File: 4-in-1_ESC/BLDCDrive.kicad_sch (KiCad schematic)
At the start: 26 parts, among them Q13 BSC070N10NS3G, Q14 BSC070N10NS3G, Q21 BSC070N10NS3G, Q22 BSC070N10NS3G, Q5 BSC070N10NS3G, Q9 BSC070N10NS3G, U1 JSM6288Q

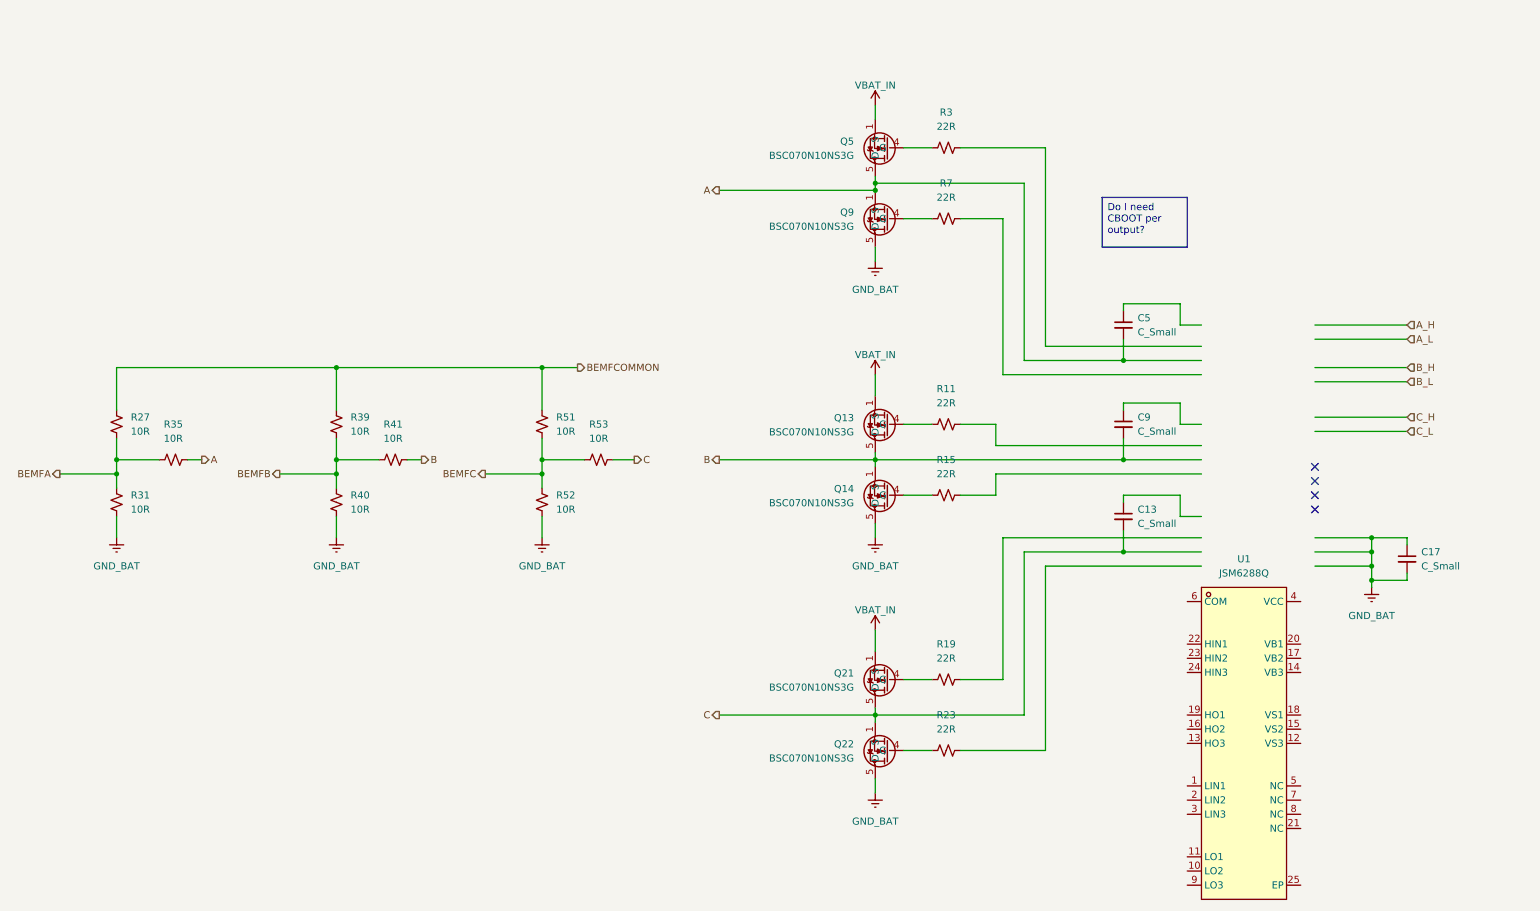
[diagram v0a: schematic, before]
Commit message: Schematic Updates
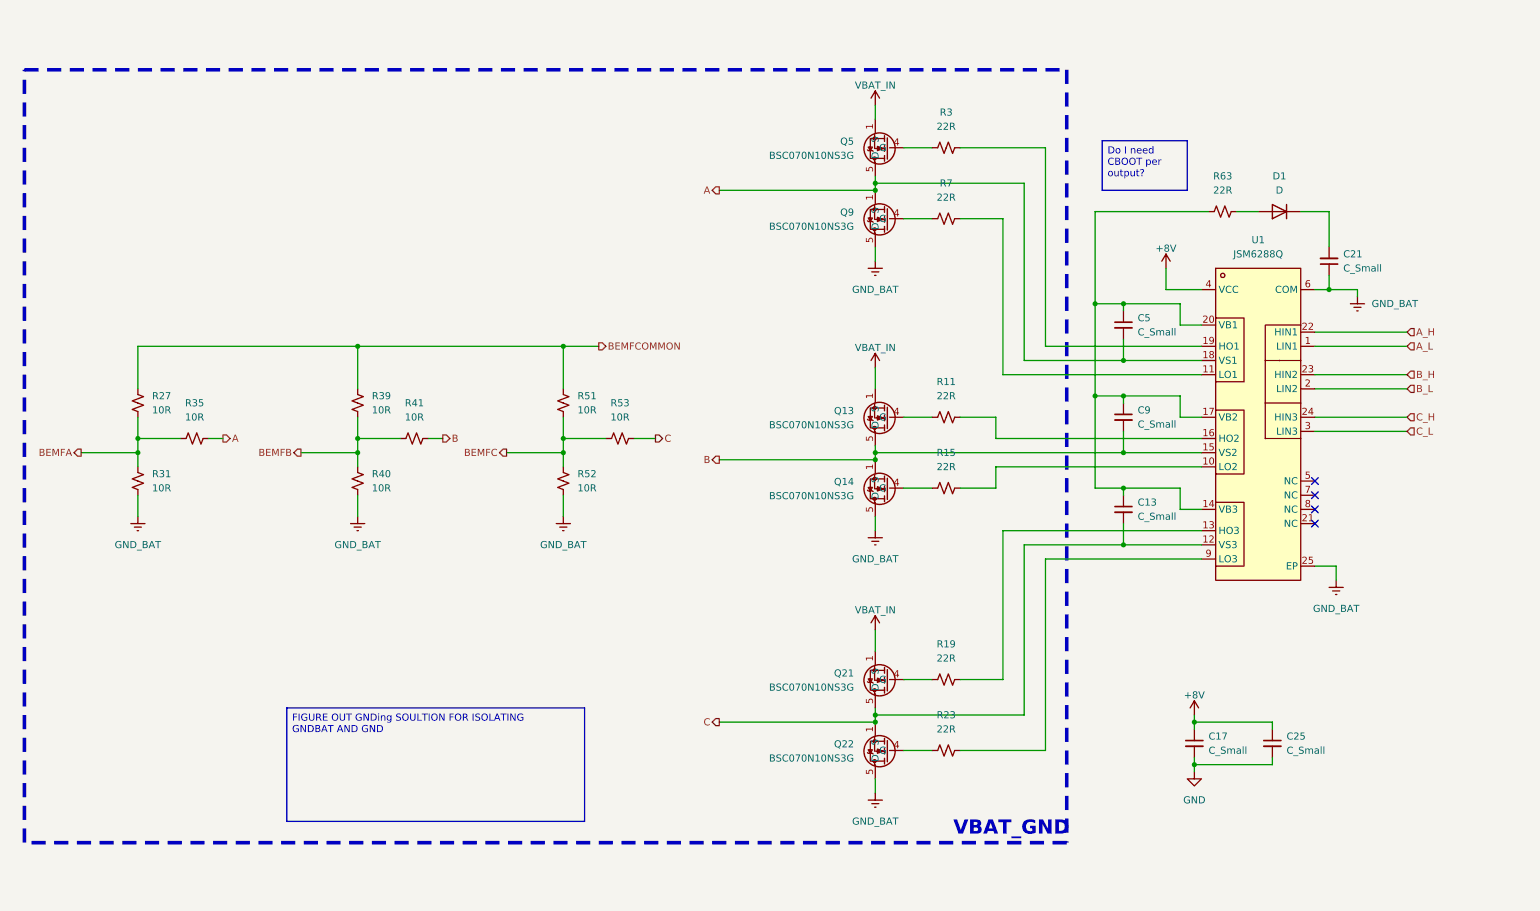
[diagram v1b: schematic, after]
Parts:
- added C21, C25: C_Small, symbol Device:C_Small
- added D1: D, symbol Device:D
- added R63: 22R, symbol Device:R_Small_US
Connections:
- net A: now also U1.18 (VS1)
- net A_H: now also U1.22 (HIN1)
- net A_L: now also U1.1 (LIN1)
- net B: now also U1.15 (VS2)
- net B_H: now also U1.23 (HIN2)
- net B_L: now also U1.2 (LIN2)
- net C: now also U1.12 (VS3)
- net C_H: now also U1.24 (HIN3)
- net C_L: now also U1.3 (LIN3)
- net GND_BAT: now also U1.25 (EP), U1.6 (COM), C21.1; no longer C17.1, C17.2
- net at C13.1: now also C5.1, C9.1, U1.14 (VB3), U1.17 (VB2), U1.20 (VB1), R63.1
- net at R11.2: now also U1.16 (HO2)
- net at R7.2: now also U1.11 (LO1)
- net at U1.10 (LO2): now also R15.2
- net at U1.13 (HO3): now also R19.2
- net at U1.19 (HO1): now also R3.2
- net +8V: now reaches U1.4 (VCC)
- net +8V: now also C17.1, C25.1
- net at U1.9 (LO3): now also R23.2
- new net: D1.2 (A), R63.2
- new net: C21.2, D1.1 (K)
- new net GND: C17.2, C25.2
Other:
- note added: "VBAT_GND"
- moved on the sheet: C13, C9, Q13, Q14, R11, R15, R27, R31, R35, R39, R40, R41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

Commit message: Schematic Updates
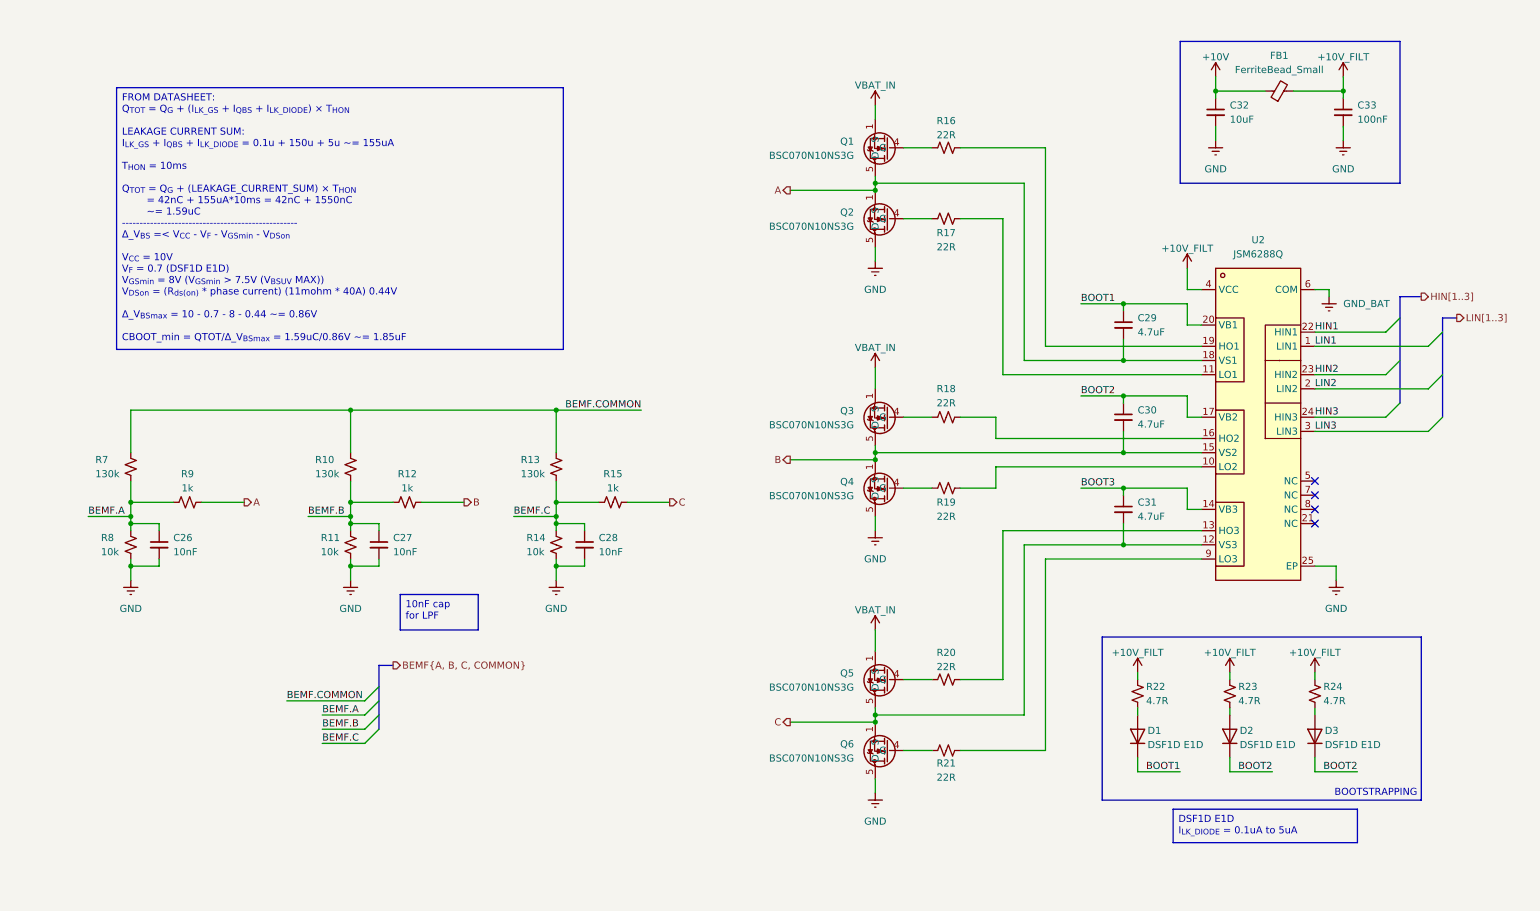
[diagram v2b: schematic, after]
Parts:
- removed C21: C_Small, symbol Device:C_Small
- removed R39, R40, R41, R51, R52, R53: 10R, symbol Device:R_Small_US
- removed R63: 22R, symbol Device:R_Small_US
- added C26, C27, C28: 10nF, Capacitor_SMD:C_0402_1005Metric, symbol Device:C_Small
- added D2, D3: DSF1D E1D, Diode_SMD:D_SOD-123F, symbol Device:D
- added FB1: FerriteBead_Small, Inductor_SMD:L_0402_1005Metric, symbol Device:FerriteBead_Small
- added R10, R13: 130k, Resistor_SMD:R_0402_1005Metric, symbol Device:R_Small_US
- added R11, R14: 10k, Resistor_SMD:R_0402_1005Metric, symbol Device:R_Small_US
- added R12, R15: 1k, Resistor_SMD:R_0402_1005Metric, symbol Device:R_Small_US
- added R22, R23, R24: 4.7R, Resistor_SMD:R_0402_1005Metric, symbol Device:R_Small_US
- C29: renamed from C5; value C_Small -> 4.7uF; footprint (none) -> Capacitor_SMD:C_0402_1005Metric
- C30: renamed from C9; value C_Small -> 4.7uF; footprint (none) -> Capacitor_SMD:C_0402_1005Metric
- C31: renamed from C13; value C_Small -> 4.7uF; footprint (none) -> Capacitor_SMD:C_0402_1005Metric
- C32: renamed from C17; value C_Small -> 10uF; footprint (none) -> Capacitor_SMD:C_0402_1005Metric
- C33: renamed from C25; value C_Small -> 100nF; footprint (none) -> Capacitor_SMD:C_0402_1005Metric
- D1: value D -> DSF1D E1D; footprint (none) -> Diode_SMD:D_SOD-123F; LCSC_Part_Number (none) -> C5365387
- R16: renamed from R3; footprint (none) -> Resistor_SMD:R_0402_1005Metric
- R17: renamed from R7; footprint (none) -> Resistor_SMD:R_0402_1005Metric
- R18: renamed from R11; footprint (none) -> Resistor_SMD:R_0402_1005Metric
- R19: renamed from R15; footprint (none) -> Resistor_SMD:R_0402_1005Metric
- R20: renamed from R19; footprint (none) -> Resistor_SMD:R_0402_1005Metric
- R21: renamed from R23; footprint (none) -> Resistor_SMD:R_0402_1005Metric
- R7: renamed from R27; value 10R -> 130k; footprint (none) -> Resistor_SMD:R_0402_1005Metric
- R8: renamed from R31; value 10R -> 10k; footprint (none) -> Resistor_SMD:R_0402_1005Metric
- R9: renamed from R35; value 10R -> 1k; footprint (none) -> Resistor_SMD:R_0402_1005Metric
- renumbered Q5 to Q1, Q9 to Q2, Q13 to Q3, Q14 to Q4, Q21 to Q5, Q22 to Q6, U1 to U2
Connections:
- net B: now also R12.1
- net C: now also R15.1
- net GND: now also Q2.5 (D), Q2.6 (D), Q2.7 (D), Q2.8 (D), Q4.5 (D), Q4.6 (D), Q4.7 (D), Q4.8 (D), Q6.5 (D), Q6.6 (D), Q6.7 (D), Q6.8 (D), R8.1, U2.25 (EP), C26.2, C27.2, C28.2, R11.1, R14.1
- net GND_BAT: no longer Q2.5 (D), Q2.6 (D), Q2.7 (D), Q2.8 (D), Q4.5 (D), Q4.6 (D), Q4.7 (D), Q4.8 (D), Q6.5 (D), Q6.6 (D), Q6.7 (D), Q6.8 (D), R8.1, U2.25 (EP)
- net at D1.2 (A): now also R22.1
- net BOOT1: now reaches D1.1 (K)
- net BOOT1: now also C29.1, U2.20 (VB1)
- net +8V renamed +10V_FILT
- net +10V_FILT: now also FB1.2, R22.2, R23.2, R24.2; no longer C32.1
- net A_H renamed HIN1
- net A_L renamed LIN1
- net BEMFA renamed BEMF.A
- net BEMF.A: now also C26.1
- net BEMFCOMMON renamed BEMF.COMMON
- net BEMF.COMMON: now also R10.2, R13.2
- net B_H renamed HIN2
- net B_L renamed LIN2
- net C_H renamed HIN3
- net C_L renamed LIN3
- new net: D3.2 (A), R24.1
- new net: D2.2 (A), R23.1
- new net +10V: C32.1, FB1.1
- new net BEMF.B: C27.1, R10.1, R11.2, R12.2
- new net BEMF.C: C28.1, R13.1, R14.2, R15.2
- new net BOOT2: C30.1, D2.1 (K), D3.1 (K), U2.17 (VB2)
- new net BOOT3: C31.1, U2.14 (VB3)
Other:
- note added: "BOOTSTRAPPING"
- note removed: "VBAT_GND"
- moved on the sheet: C32, C33, R7, R8, R9

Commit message: Schematic First Pass
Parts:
- removed FB1: FerriteBead_Small, Inductor_SMD:L_0402_1005Metric, symbol Device:FerriteBead_Small
- removed R10, R13, R7: 130k, Resistor_SMD:R_0402_1005Metric, symbol Device:R_Small_US
- removed R12, R15, R9: 1k, Resistor_SMD:R_0402_1005Metric, symbol Device:R_Small_US
- added C54: 100nF, Capacitor_SMD:C_0402_1005Metric, symbol Device:C_Small
- added C67: 4.7uF, Capacitor_SMD:C_0402_1005Metric, symbol Device:C_Small
- added FB7: 600Ω@100MHz, Inductor_SMD:L_0402_1005Metric, symbol Device:FerriteBead_Small
- added R45, R67, R96: 110k, Resistor_SMD:R_0402_1005Metric, symbol Device:R_Small_US
- added R49, R82, R90: 10k, Resistor_SMD:R_0402_1005Metric, symbol Device:R_Small_US
- R22, R23, R24: value 4.7R -> 2.2R
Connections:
- net +10V: now also R22.2, R23.2, R24.2, C54.1, FB7.1
- net +10V_FILT: now also C67.1, FB7.2; no longer R22.2, R23.2, R24.2
- net A: now also R45.2
- net B: now also R67.2
- net BEMF.A: now also R45.1, R49.1
- net BEMF.B: now also R67.1, R82.1
- net BEMF.C: now also R90.1, R96.1
- net BEMF.COMMON: now also R49.2, R82.2, R90.2
- net C: now also R96.2
- net GND: now also C54.2, C67.2
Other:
- note added: "3 PHASE GATE DRIVER"
- note added: "FILTERING"
- note added: "JSMSEMI JSM6288Q"
- note added: "Three-phase high and low side power MOSFET/IGBT driver chip"
- moved on the sheet: C26, C27, C28, C32, C33, R11, R14, R8
